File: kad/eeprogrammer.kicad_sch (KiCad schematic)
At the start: 16 parts, among them J1 Conn_01x04_Female, U2 28C256, U3 74HC595, U4 74HC595, U5 AT25xxx, U6 24LC256

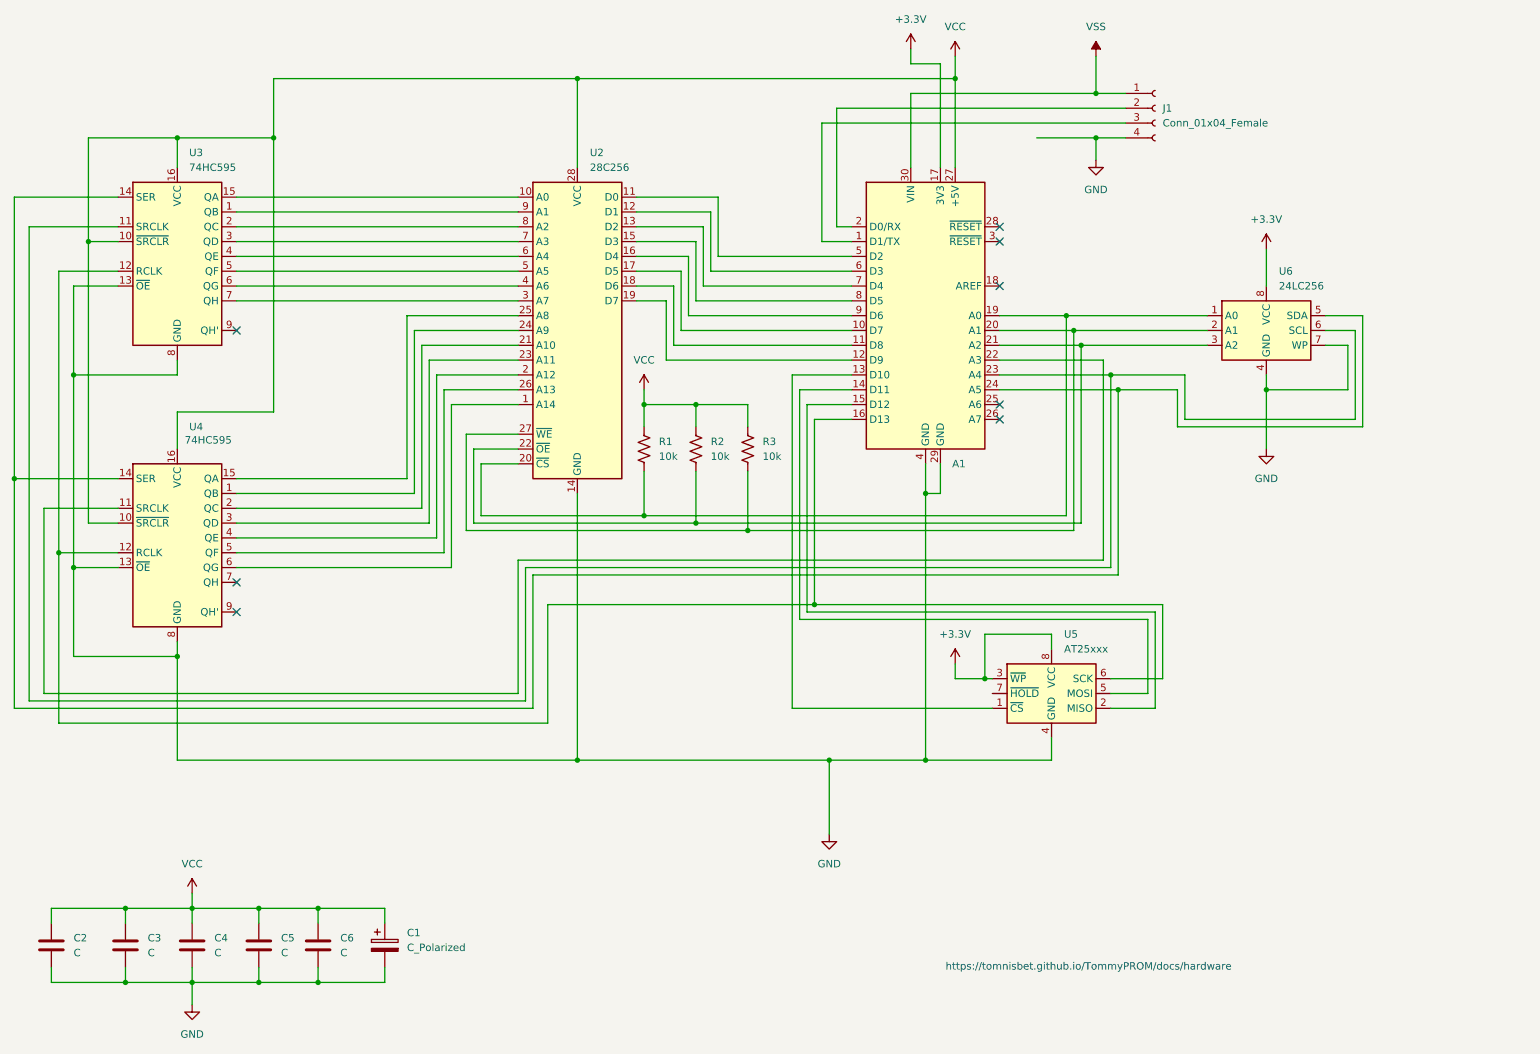
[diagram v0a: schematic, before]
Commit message: added kicad eeprogrammer
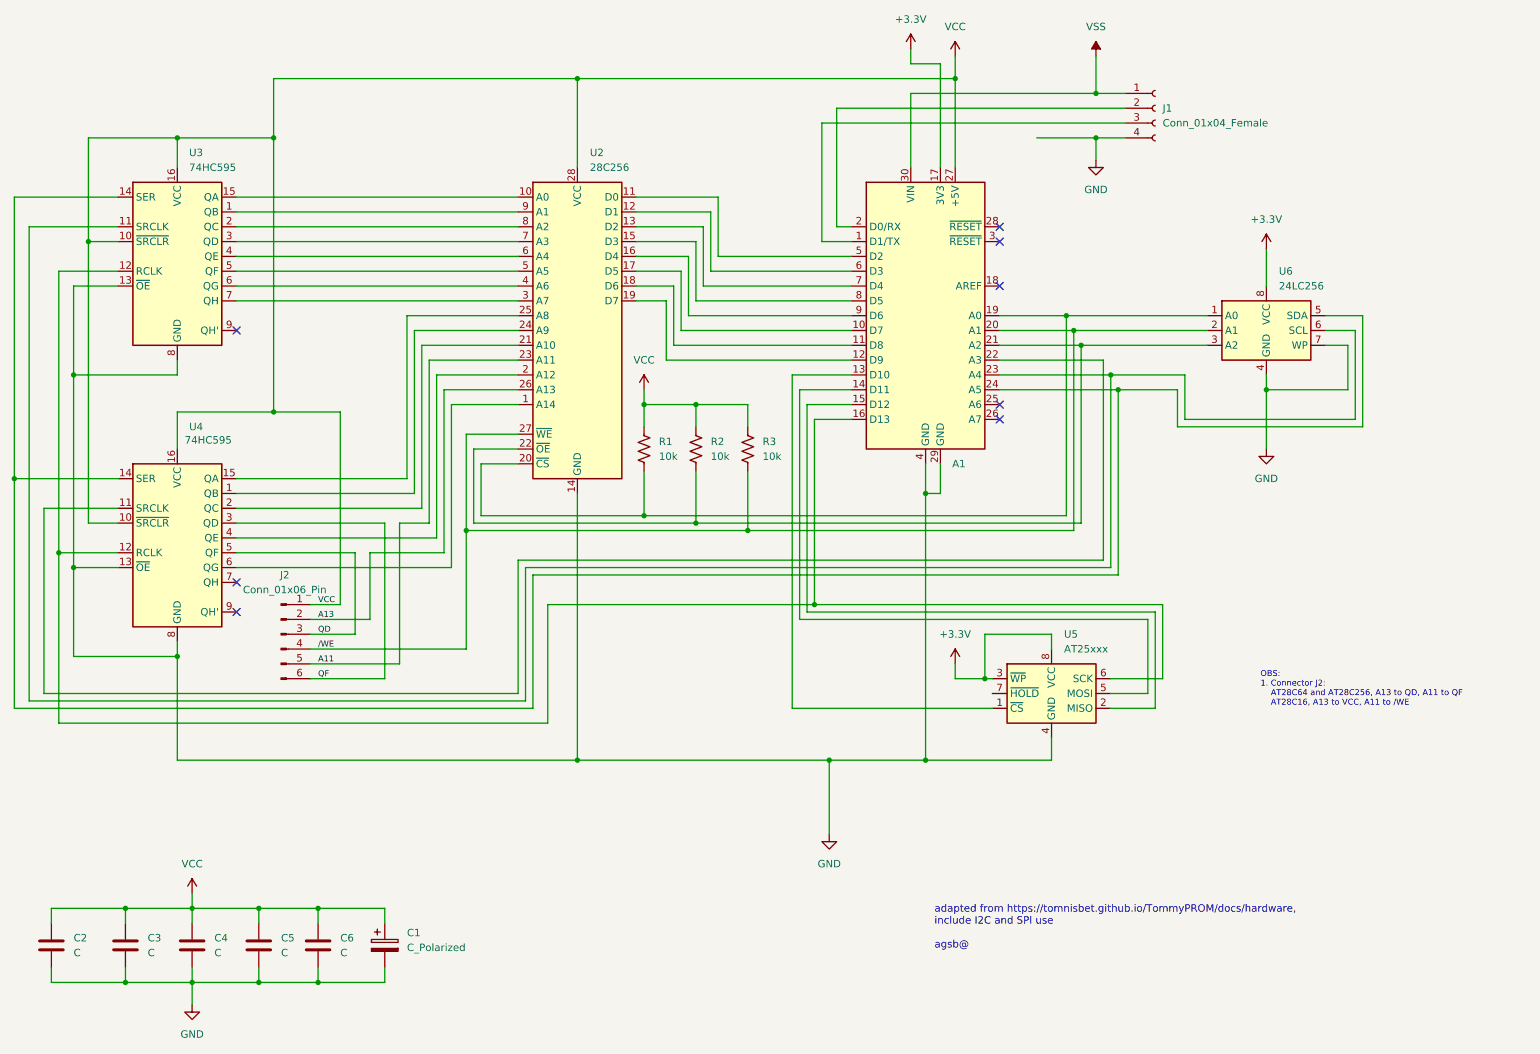
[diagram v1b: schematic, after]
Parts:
- added J2: Conn_01x06_Pin, symbol Connector:Conn_01x06_Pin
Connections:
- net VCC: now also J2.1 (Pin_1)
- net A11: now reaches U2.23 (A11)
- net A11: now also J2.5 (Pin_5); no longer U4.3 (QD)
- net A13: now reaches U2.26 (A13)
- net A13: now also J2.2 (Pin_2); no longer U4.5 (QF)
- net /WE: now reaches A1.20 (A1), R3.2, U2.27 (~{WE}), U6.2 (A1)
- net /WE: now also J2.4 (Pin_4)
- new net QD: J2.3 (Pin_3), U4.5 (QF)
- new net QF: J2.6 (Pin_6), U4.3 (QD)
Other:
- note added: "OBS: 1. Connector J2: AT28C64 and AT28C256, A13 to QD, A11 to QF AT28C16, A13 to VCC, A11 to /WE"
- note added: "adapted from https://tomnisbet.github.io/TommyPROM/docs/hardware, include I2C and SPI use agsb@"
- note removed: "https://tomnisbet.github.io/TommyPROM/docs/hardware"

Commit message: added kicad eeprogrammer
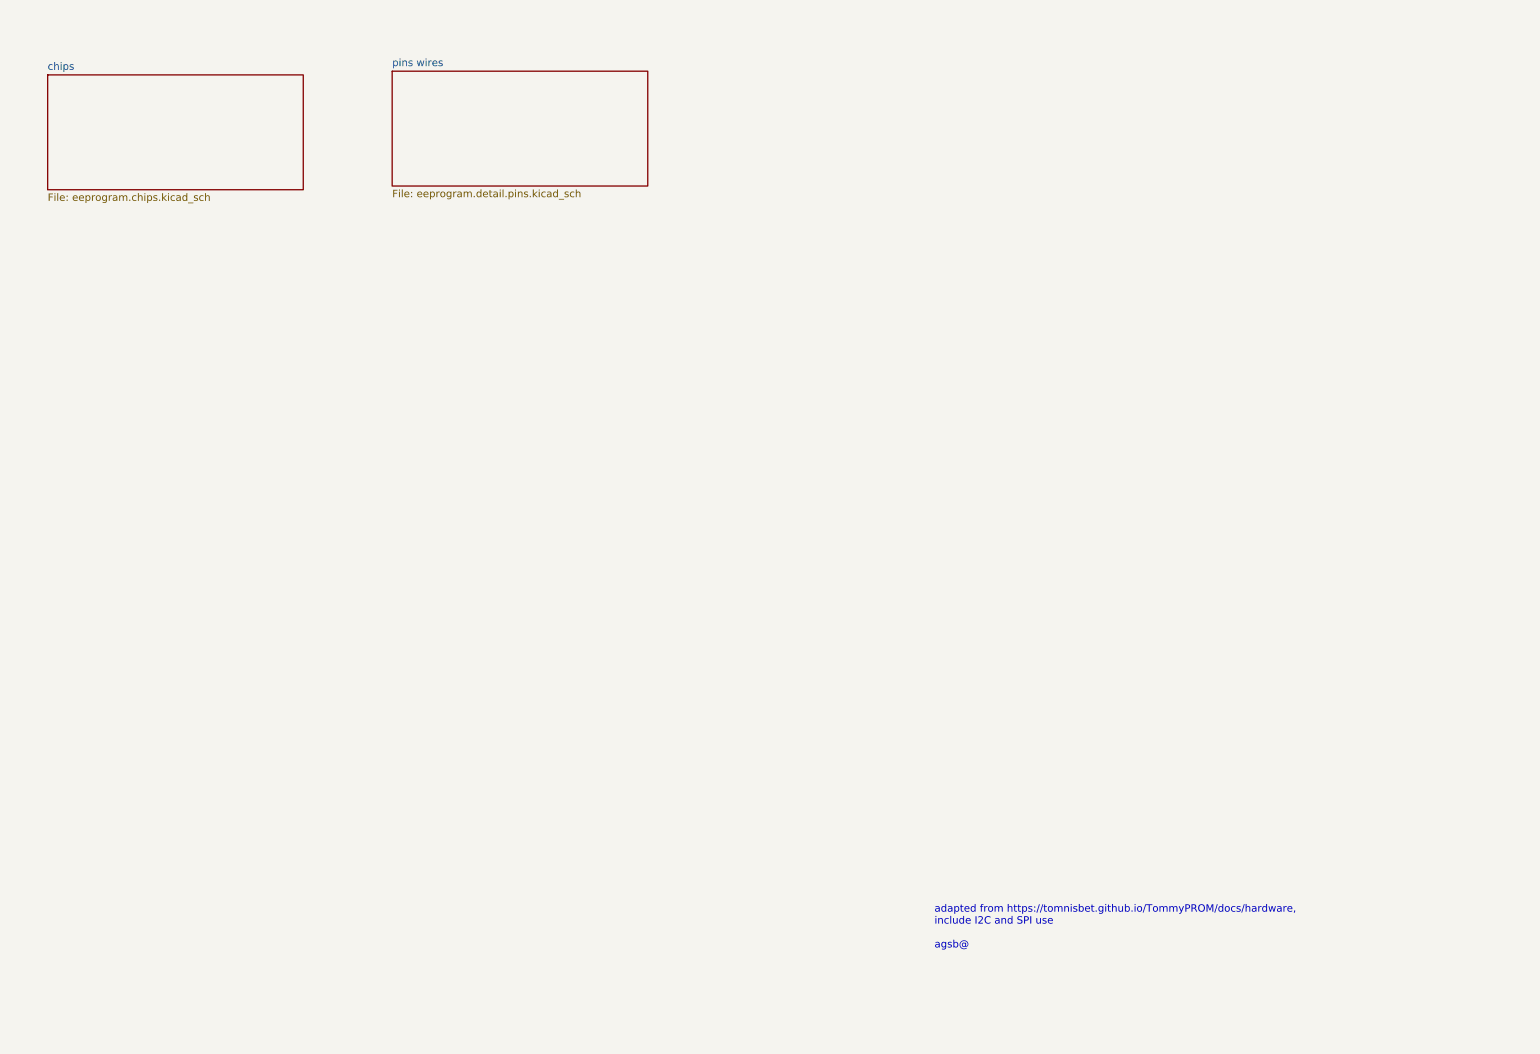
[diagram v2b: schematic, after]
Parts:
- removed A1: Arduino_Nano_v2.x, Module:Arduino_Nano, symbol MCU_Module:Arduino_Nano_v2.x
- removed C1: C_Polarized, symbol Device:C_Polarized
- removed C2, C3, C4, C5, C6: C, symbol Device:C
- removed J1: Conn_01x04_Female, symbol Connector:Conn_01x04_Female
- removed J2: Conn_01x06_Pin, symbol Connector:Conn_01x06_Pin
- removed R1, R2, R3: 10k, symbol Device:R_US
- removed U2: 28C256, symbol Memory_EEPROM:28C256
- removed U3, U4: 74HC595, symbol 74xx:74HC595
- removed U5: AT25xxx, symbol Memory_EEPROM:AT25xxx
- removed U6: 24LC256, symbol Memory_EEPROM:24LC256
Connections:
- no-connect marks 8 -> 0
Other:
- added sheet chips (eeprogram.chips.kicad_sch)
- added sheet pins wires (eeprogram.detail.pins.kicad_sch)
- note removed: "OBS: 1. Connector J2: AT28C64 and AT28C256, A13 to QD, A11 to QF AT28C16, A13 to VCC, A11 to /WE"
